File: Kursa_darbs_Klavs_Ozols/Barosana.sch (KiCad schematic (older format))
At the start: 15 parts, among them U2 L7808, U3 ICL7660SIPAZ, U4 ICL7660SIPAZ, U5 ICL7660SIPAZ, U6 ICL7660SIPAZ

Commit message: Shii ir 2. iteraacija kursa darbam!
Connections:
- net +8V_1: now also C11.1, C12.1, C13.1, C14.1; no longer C11.2, C12.2, C13.2, C14.2
- net -8V: now also C14.2; no longer C14.1
- net -8V_1: now also C12.2; no longer C12.1
- net -8V_2: now also C11.2; no longer C11.1
- net -8V_3: now also C13.2; no longer C13.1
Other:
- moved on the sheet: C11, C12, C13, C14
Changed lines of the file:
@@
 L CP1 C14
 U 1 1 5AFF755C
-P 5600 1200
-F 0 "C14" H 5625 1300 50  0000 L CNN
-F 1 "470 uF" H 5625 1100 50  0000 L CNN
-F 2 "" H 5600 1200 50  0001 C CNN
-F 3 "" H 5600 1200 50  0001 C CNN
-	1    5600 1200
-	1    0    0    -1
-$EndComp
-Wire Wire Line
-	5550 2300 5550 1350
+P 5850 1300
+F 0 "C14" H 5875 1400 50  0000 L CNN
+F 1 "470 uF" H 5875 1200 50  0000 L CNN
+F 2 "" H 5850 1300 50  0001 C CNN
+F 3 "" H 5850 1300 50  0001 C CNN
+	1    5850 1300
+	-1   0    0    1
+$EndComp
 Wire Wire Line
 	5250 1050 6750 1050
@@
 	3600 650  6750 650
 Connection ~ 3600 1050
-Connection ~ 5600 1050
-Connection ~ 5600 1350
 Text HLabel 6750 650  2    60   Output ~ 0
 +8V
 Text HLabel 6750 1050 2    60   Output ~ 0
 -8V
-Wire Wire Line
-	5550 1350 5600 1350
-Connection ~ 3150 1200
 Connection ~ 3300 2050
 $Comp
@@
 Wire Wire Line
 	3300 3900 5450 3900
-Wire Wire Line
-	5450 3900 5450 2900
 Connection ~ 3300 3900
 $Comp
 L CP1 C12
 U 1 1 5B0060F9
-P 5450 2750
-F 0 "C12" H 5475 2850 50  0000 L CNN
-F 1 "470 uF" H 5475 2650 50  0000 L CNN
-F 2 "" H 5450 2750 50  0001 C CNN
-F 3 "" H 5450 2750 50  0001 C CNN
-	1    5450 2750
-	1    0    0    -1
+P 5700 2850
+F 0 "C12" H 5725 2950 50  0000 L CNN
+F 1 "470 uF" H 5725 2750 50  0000 L CNN
+F 2 "" H 5700 2850 50  0001 C CNN
+F 3 "" H 5700 2850 50  0001 C CNN
+	1    5700 2850
+	-1   0    0    1
 $EndComp
 Wire Wire Line
@@
 Text HLabel 6900 2600 2    60   Output ~ 0
 -8V_1
-Connection ~ 5450 2600
 Wire Wire Line
 	3150 2350 6900 2350
@@
 L CP1 C11
 U 1 1 5B02199A
-P 5400 4400
-F 0 "C11" H 5425 4500 50  0000 L CNN
-F 1 "470 uF" H 5425 4300 50  0000 L CNN
-F 2 "" H 5400 4400 50  0001 C CNN
-F 3 "" H 5400 4400 50  0001 C CNN
-	1    5400 4400
-	1    0    0    -1
+P 5650 4450
+F 0 "C11" H 5675 4550 50  0000 L CNN
+F 1 "470 uF" H 5675 4350 50  0000 L CNN
+F 2 "" H 5650 4450 50  0001 C CNN
+F 3 "" H 5650 4450 50  0001 C CNN
+	1    5650 4450
+	-1   0    0    1
 $EndComp
 Wire Wire Line
@@
 	3150 4000 6700 4000
 Connection ~ 3150 4000
-Connection ~ 5400 4250
 $Comp
 L ICL7660SIPAZ U6
@@
 L CP1 C13
 U 1 1 5B038988
-P 5500 6050
-F 0 "C13" H 5525 6150 50  0000 L CNN
-F 1 "470 uF" H 5525 5950 50  0000 L CNN
-F 2 "" H 5500 6050 50  0001 C CNN
-F 3 "" H 5500 6050 50  0001 C CNN
-	1    5500 6050
-	1    0    0    -1
+P 5750 6100
+F 0 "C13" H 5775 6200 50  0000 L CNN
+F 1 "470 uF" H 5775 6000 50  0000 L CNN
+F 2 "" H 5750 6100 50  0001 C CNN
+F 3 "" H 5750 6100 50  0001 C CNN
+	1    5750 6100
+	-1   0    0    1
 $EndComp
 Wire Wire Line
@@
 Wire Wire Line
 	5900 5850 6000 5850
-Connection ~ 5500 5900
 Text HLabel 6000 5650 2    60   Output ~ 0
 +8V_3
@@
 Wire Wire Line
 	3150 5950 3900 5950
+Wire Wire Line
+	5750 1150 5750 1050
+Connection ~ 5750 1050
+Wire Wire Line
+	5550 1450 5850 1450
+Connection ~ 5550 1450
+Wire Wire Line
+	5550 2300 5550 1450
+Wire Wire Line
+	5650 2600 5650 2700
+Connection ~ 5650 2600
+Wire Wire Line
+	5450 3000 5700 3000
+Connection ~ 5450 3000
+Wire Wire Line
+	5450 3900 5450 3000
+Wire Wire Line
+	5650 5900 5650 5950
+Connection ~ 5650 5900
+Wire Wire Line
+	5500 6250 5750 6250
+Wire Wire Line
+	5500 6200 5500 6250
+Wire Wire Line
+	5650 4300 5650 4250
+Connection ~ 5650 4250
+Wire Wire Line
+	5650 4600 5500 4600
+Wire Wire Line
+	5500 4600 5500 4550
+Wire Wire Line
+	5500 4550 5400 4550
+Wire Wire Line
+	5650 2700 5700 2700
+Wire Wire Line
+	5850 1150 5750 1150
+Wire Wire Line
+	5650 5950 5750 5950
 $EndSCHEMATC

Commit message: Shii ir kursa darba 3. iteraacija
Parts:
- C10, C11, C12, C13, C14, C7, C8, C9: footprint (none) -> Capacitors_THT:CP_Radial_D10.0mm_P5.00mm
- C5, C6: footprint (none) -> Capacitors_THT:C_Axial_L3.8mm_D2.6mm_P7.50mm_Horizontal
- U2: footprint (none) -> TO_SOT_Packages_THT:TO-220_Vertical
- U3, U4, U5, U6: footprint DIP254P762X533-8 -> ICL7660SIPAZ:DIP254P762X533-8
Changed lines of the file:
@@
 F 0 "U2" H 2200 1325 50  0000 C CNN
 F 1 "L7808" H 2350 1325 50  0000 L CNN
-F 2 "" H 2375 1050 50  0001 L CIN
-F 3 "" H 2350 1150 50  0001 C CNN
+F 2 "TO_SOT_Packages_THT:TO-220_Vertical" H 2375 1050 50  0001 L CIN
+F 3 "https://eu.mouser.com/datasheet/2/389/lm217-974117.pdf" H 2350 1150 50  0001 C CNN
 	1    2350 1200
 	1    0    0    -1
@@
 F 0 "C5" H 1925 1500 50  0000 L CNN
 F 1 "100 nF" H 1925 1300 50  0000 L CNN
-F 2 "" H 1938 1250 50  0001 C CNN
-F 3 "" H 1900 1400 50  0001 C CNN
+F 2 "Capacitors_THT:C_Axial_L3.8mm_D2.6mm_P7.50mm_Horizontal" H 1938 1250 50  0001 C CNN
+F 3 "https://eu.mouser.com/datasheet/2/427/maseries-1211360.pdf" H 1900 1400 50  0001 C CNN
 	1    1900 1400
 	1    0    0    -1
@@
 F 0 "C6" H 2875 1500 50  0000 L CNN
 F 1 "100 nF" H 2875 1300 50  0000 L CNN
-F 2 "" H 2888 1250 50  0001 C CNN
-F 3 "" H 2850 1400 50  0001 C CNN
+F 2 "Capacitors_THT:C_Axial_L3.8mm_D2.6mm_P7.50mm_Horizontal" H 2888 1250 50  0001 C CNN
+F 3 "https://eu.mouser.com/datasheet/2/427/maseries-1211360.pdf" H 2850 1400 50  0001 C CNN
 	1    2850 1400
 	1    0    0    -1
@@
 F 0 "U3" H 4550 1950 50  0000 L BNN
 F 1 "ICL7660SIPAZ" H 4350 700 50  0000 L BNN
-F 2 "DIP254P762X533-8" H 4550 1450 50  0001 L BNN
+F 2 "ICL7660SIPAZ:DIP254P762X533-8" H 4550 1450 50  0001 L BNN
 F 3 "Good" H 4550 1450 50  0001 L BNN
 F 4 "ICL7660SIPAZ" H 4550 1450 50  0001 L BNN "Field4"
@@
 F 0 "C7" H 3575 1600 50  0000 L CNN
 F 1 "10 uF" H 3300 1400 50  0000 L CNN
-F 2 "" H 3550 1500 50  0001 C CNN
-F 3 "" H 3550 1500 50  0001 C CNN
+F 2 "Capacitors_THT:CP_Radial_D10.0mm_P5.00mm" H 3550 1500 50  0001 C CNN
+F 3 "https://eu.mouser.com/datasheet/2/293/e-upx-876312.pdf" H 3550 1500 50  0001 C CNN
 	1    3550 1500
 	1    0    0    -1
@@
 F 0 "C14" H 5875 1400 50  0000 L CNN
 F 1 "470 uF" H 5875 1200 50  0000 L CNN
-F 2 "" H 5850 1300 50  0001 C CNN
-F 3 "" H 5850 1300 50  0001 C CNN
+F 2 "Capacitors_THT:CP_Radial_D10.0mm_P5.00mm" H 5850 1300 50  0001 C CNN
+F 3 "https://eu.mouser.com/datasheet/2/427/517d-239964.pdf" H 5850 1300 50  0001 C CNN
 	1    5850 1300
 	-1   0    0    1
@@
 F 0 "U4" H 4550 3500 50  0000 L BNN
 F 1 "ICL7660SIPAZ" H 4350 2250 50  0000 L BNN
-F 2 "DIP254P762X533-8" H 4550 3000 50  0001 L BNN
+F 2 "ICL7660SIPAZ:DIP254P762X533-8" H 4550 3000 50  0001 L BNN
 F 3 "Good" H 4550 3000 50  0001 L BNN
 F 4 "ICL7660SIPAZ" H 4550 3000 50  0001 L BNN "Field4"
@@
 F 0 "C8" H 3625 3150 50  0000 L CNN
 F 1 "10 uF" H 3350 2950 50  0000 L CNN
-F 2 "" H 3600 3050 50  0001 C CNN
-F 3 "" H 3600 3050 50  0001 C CNN
+F 2 "Capacitors_THT:CP_Radial_D10.0mm_P5.00mm" H 3600 3050 50  0001 C CNN
+F 3 "https://eu.mouser.com/datasheet/2/293/e-upx-876312.pdf" H 3600 3050 50  0001 C CNN
 	1    3600 3050
 	1    0    0    -1
@@
 F 0 "C12" H 5725 2950 50  0000 L CNN
 F 1 "470 uF" H 5725 2750 50  0000 L CNN
-F 2 "" H 5700 2850 50  0001 C CNN
-F 3 "" H 5700 2850 50  0001 C CNN
+F 2 "Capacitors_THT:CP_Radial_D10.0mm_P5.00mm" H 5700 2850 50  0001 C CNN
+F 3 "https://eu.mouser.com/datasheet/2/427/517d-239964.pdf" H 5700 2850 50  0001 C CNN
 	1    5700 2850
 	-1   0    0    1
@@
 F 0 "U5" H 4550 5150 50  0000 L BNN
 F 1 "ICL7660SIPAZ" H 4350 3900 50  0000 L BNN
-F 2 "DIP254P762X533-8" H 4550 4650 50  0001 L BNN
+F 2 "ICL7660SIPAZ:DIP254P762X533-8" H 4550 4650 50  0001 L BNN
 F 3 "Good" H 4550 4650 50  0001 L BNN
 F 4 "ICL7660SIPAZ" H 4550 4650 50  0001 L BNN "Field4"
@@
 F 0 "C9" H 3625 4850 50  0000 L CNN
 F 1 "10 uF" H 3350 4650 50  0000 L CNN
-F 2 "" H 3600 4750 50  0001 C CNN
-F 3 "" H 3600 4750 50  0001 C CNN
+F 2 "Capacitors_THT:CP_Radial_D10.0mm_P5.00mm" H 3600 4750 50  0001 C CNN
+F 3 "https://eu.mouser.com/datasheet/2/293/e-upx-876312.pdf" H 3600 4750 50  0001 C CNN
 	1    3600 4750
 	1    0    0    -1
@@
 F 0 "C11" H 5675 4550 50  0000 L CNN
 F 1 "470 uF" H 5675 4350 50  0000 L CNN
-F 2 "" H 5650 4450 50  0001 C CNN
-F 3 "" H 5650 4450 50  0001 C CNN
+F 2 "Capacitors_THT:CP_Radial_D10.0mm_P5.00mm" H 5650 4450 50  0001 C CNN
+F 3 "https://eu.mouser.com/datasheet/2/427/517d-239964.pdf" H 5650 4450 50  0001 C CNN
 	1    5650 4450
 	-1   0    0    1
@@
 F 0 "U6" H 4600 6850 50  0000 L BNN
 F 1 "ICL7660SIPAZ" H 4400 5600 50  0000 L BNN
-F 2 "DIP254P762X533-8" H 4600 6350 50  0001 L BNN
+F 2 "ICL7660SIPAZ:DIP254P762X533-8" H 4600 6350 50  0001 L BNN
 F 3 "Good" H 4600 6350 50  0001 L BNN
 F 4 "ICL7660SIPAZ" H 4600 6350 50  0001 L BNN "Field4"
@@
 F 0 "C10" H 3725 6500 50  0000 L CNN
 F 1 "10 uF" H 3450 6300 50  0000 L CNN
-F 2 "" H 3700 6400 50  0001 C CNN
-F 3 "" H 3700 6400 50  0001 C CNN
+F 2 "Capacitors_THT:CP_Radial_D10.0mm_P5.00mm" H 3700 6400 50  0001 C CNN
+F 3 "https://eu.mouser.com/datasheet/2/293/e-upx-876312.pdf" H 3700 6400 50  0001 C CNN
 	1    3700 6400
 	1    0    0    -1
@@
 F 0 "C13" H 5775 6200 50  0000 L CNN
 F 1 "470 uF" H 5775 6000 50  0000 L CNN
-F 2 "" H 5750 6100 50  0001 C CNN
-F 3 "" H 5750 6100 50  0001 C CNN
+F 2 "Capacitors_THT:CP_Radial_D10.0mm_P5.00mm" H 5750 6100 50  0001 C CNN
+F 3 "https://eu.mouser.com/datasheet/2/427/517d-239964.pdf" H 5750 6100 50  0001 C CNN
 	1    5750 6100
 	-1   0    0    1

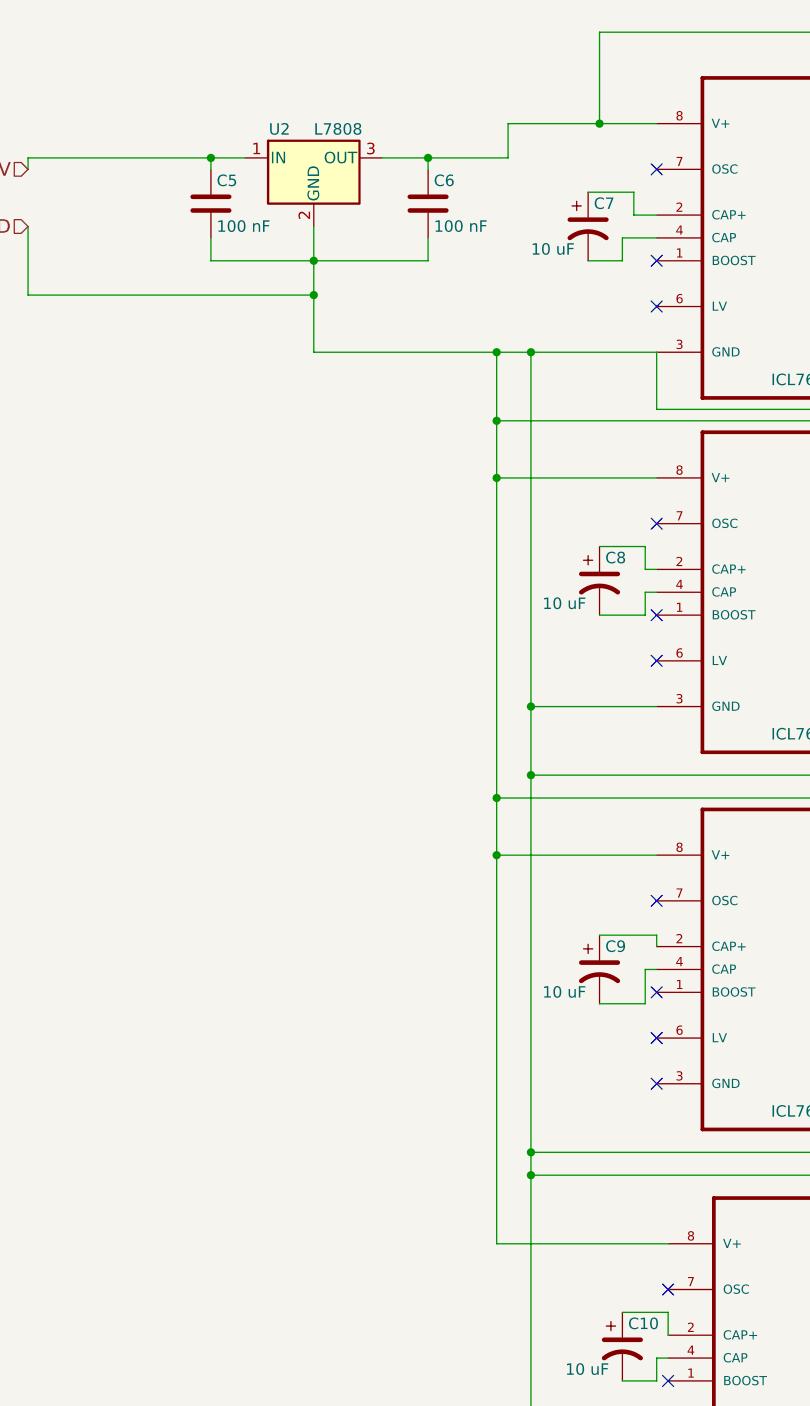
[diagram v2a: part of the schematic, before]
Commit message: Kursa darba plates 4. iteraacija
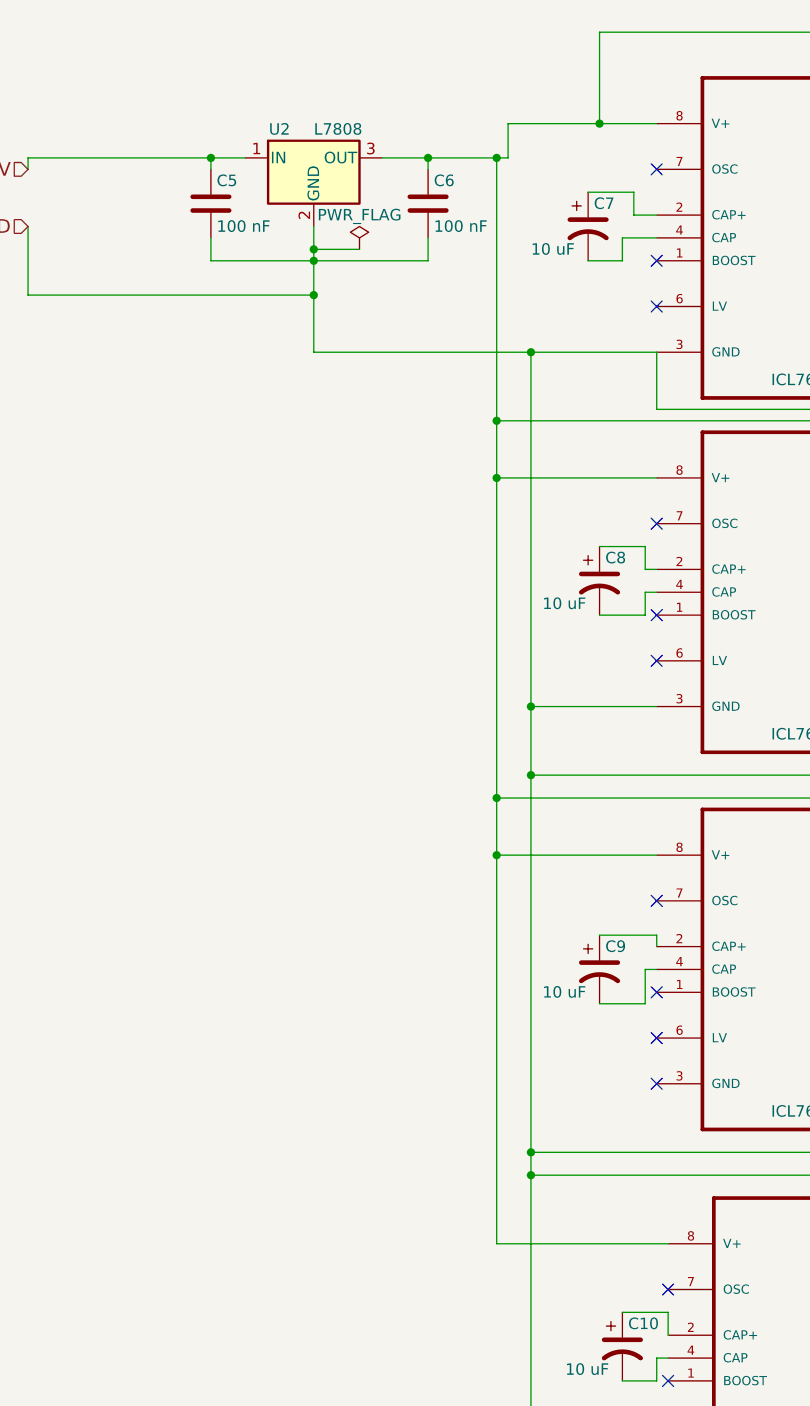
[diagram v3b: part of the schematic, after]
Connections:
- net +8V: now also U4.8 (V+), U5.8 (V+), U6.8 (V+)
- net +8V_1 renamed +8V_3
- net +8V_3: no longer U4.8 (V+), U5.8 (V+), U6.8 (V+)
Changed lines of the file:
@@
 Connection ~ 3300 6900
 Wire Wire Line
-	3150 2050 3150 5950
-Connection ~ 3150 2050
+	3150 1200 3150 5950
 Wire Wire Line
 	3900 6350 3900 6250
@@
 Wire Wire Line
 	5650 5950 5750 5950
+Connection ~ 3150 1200
+$Comp
+L PWR_FLAG #FLG04
+U 1 1 5B13D791
+P 2550 1600
+F 0 "#FLG04" H 2550 1675 50  0001 C CNN
+F 1 "PWR_FLAG" H 2550 1750 50  0000 C CNN
+F 2 "" H 2550 1600 50  0001 C CNN
+F 3 "" H 2550 1600 50  0001 C CNN
+	1    2550 1600
+	1    0    0    -1
+$EndComp
+Wire Wire Line
+	2550 1600 2350 1600
+Connection ~ 2350 1600
 $EndSCHEMATC
